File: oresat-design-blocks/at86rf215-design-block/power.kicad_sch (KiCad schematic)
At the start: 32 parts, among them J2 U.FL, J3 Conn_01x04, J4 Conn_01x04, J5 Conn_01x07, J6 Conn_01x10, U1 AT86RF215, Y1 TXETACSANF-26.000000

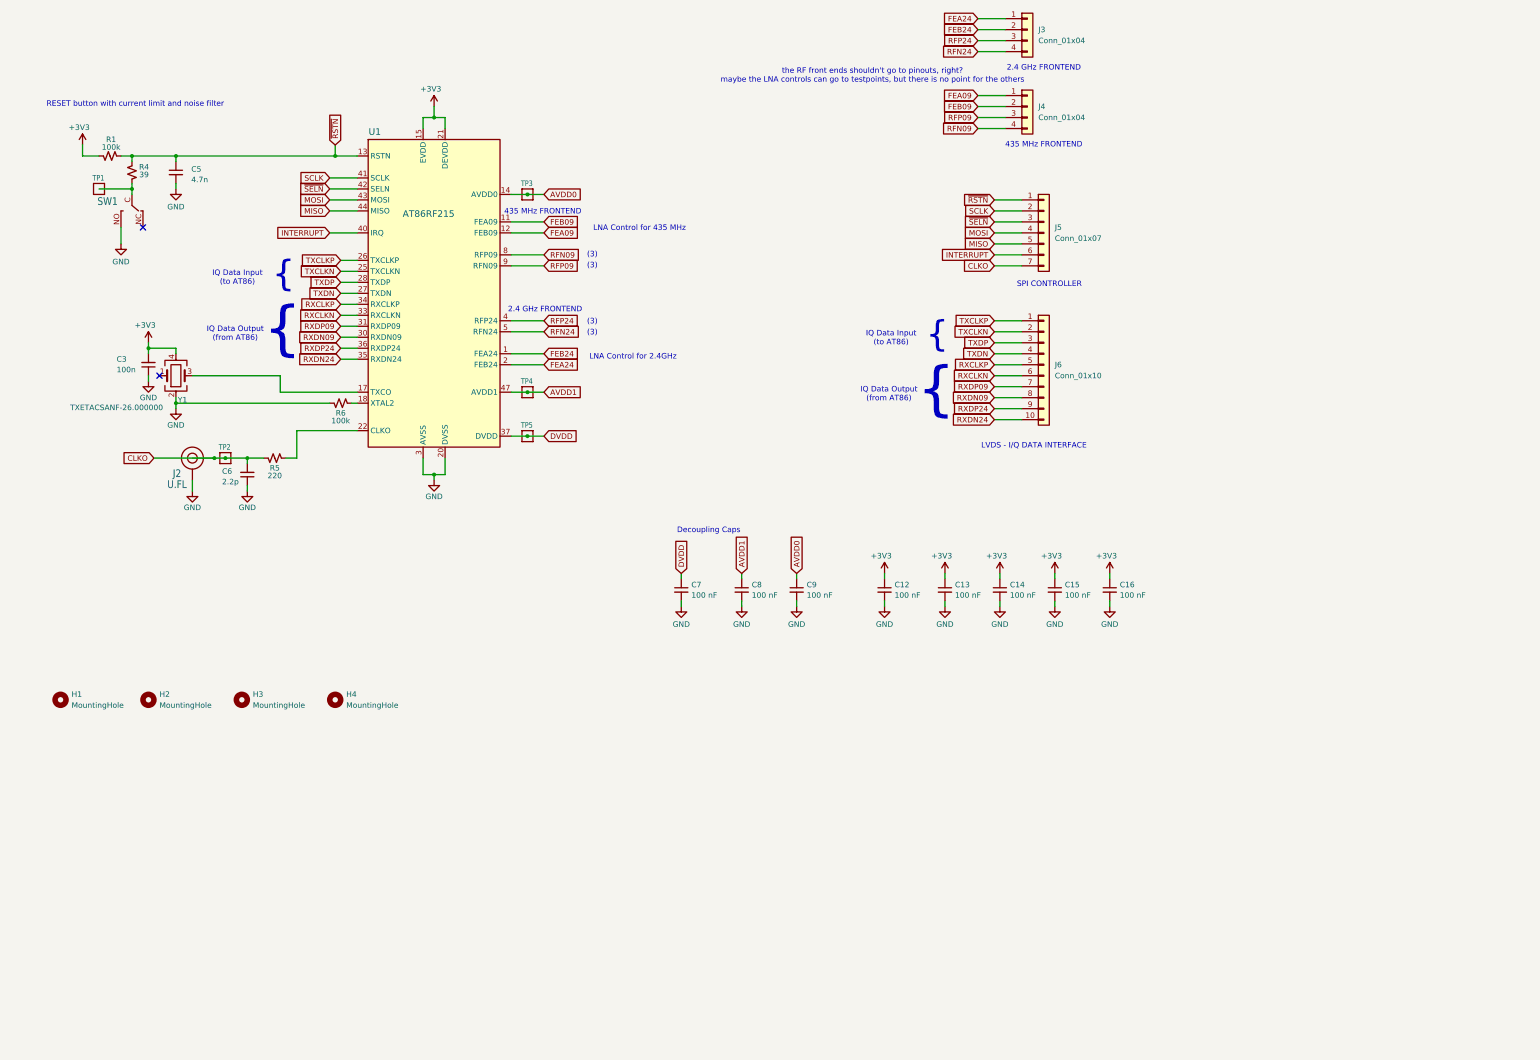
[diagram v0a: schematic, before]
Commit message: added initial footprints and oreganized schematic. Started PCB
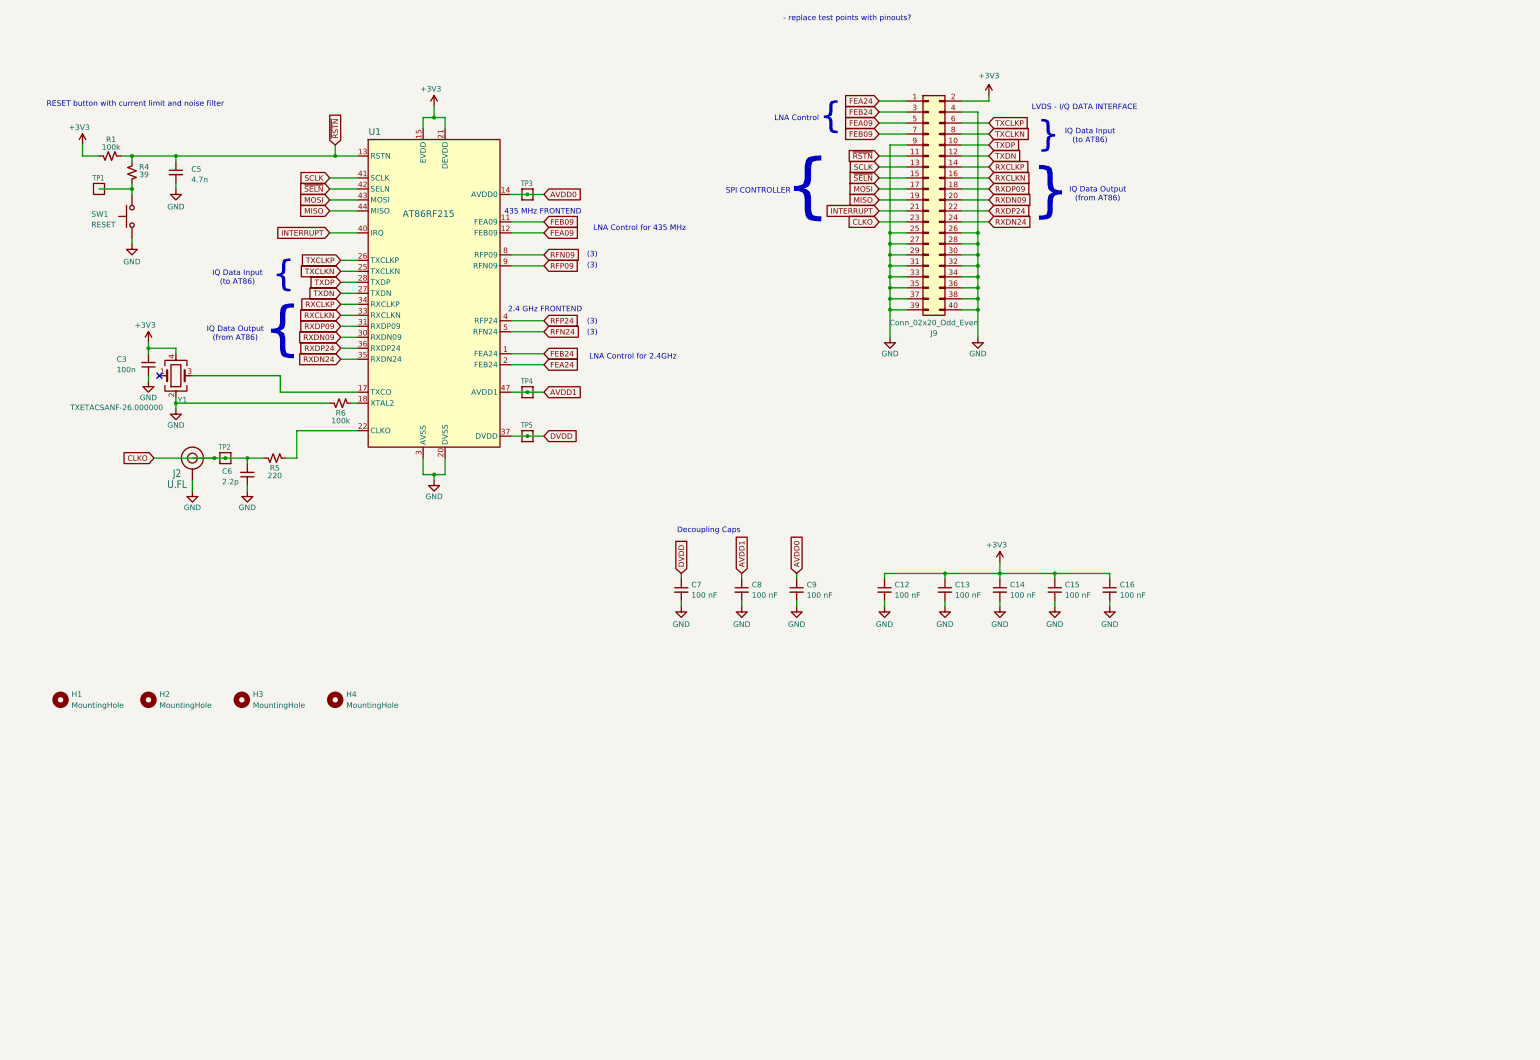
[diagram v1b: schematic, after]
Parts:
- removed J3, J4: Conn_01x04, symbol Connector_Generic:Conn_01x04
- removed J5: Conn_01x07, symbol Connector_Generic:Conn_01x07
- removed J6: Conn_01x10, symbol Connector_Generic:Conn_01x10
- removed SW1: ~, oresat-misc:D2F-L3-D-HORIZONTAL-R, symbol oresat-misc:OMRON-D2F-L3-D-RIGHT
- added J9: Conn_02x20_Odd_Even, Connector_PinHeader_2.54mm:PinHeader_2x20_P2.54mm_Vertical, symbol Connector_Generic:Conn_02x20_Odd_Even
- added SW1: RESET, Button_Switch_THT:SW_PUSH_6mm, symbol Switch:SW_Push
- C12, C13, C14, C15, C16, C3, C5, C6, C7, C8, C9: footprint (none) -> Capacitor_SMD:C_0603_1608Metric
- H1, H2, H3, H4: footprint (none) -> oresat-misc:M2-Press-Fit-Nut
- R1, R4, R5, R6: footprint (none) -> Resistor_SMD:R_0603_1608Metric
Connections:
- net +3V3: now also J9.2 (Pin_2)
- net AVSS: now also J9.25 (Pin_25), J9.26 (Pin_26), J9.27 (Pin_27), J9.28 (Pin_28), J9.29 (Pin_29), J9.30 (Pin_30), J9.31 (Pin_31), J9.32 (Pin_32), J9.33 (Pin_33), J9.34 (Pin_34), J9.35 (Pin_35), J9.36 (Pin_36), J9.37 (Pin_37), J9.38 (Pin_38), J9.39 (Pin_39), J9.4 (Pin_4), J9.40 (Pin_40), J9.9 (Pin_9), SW1.2
- net CLKO: now also J9.23 (Pin_23)
- net FEA09: now also J9.5 (Pin_5)
- net FEA24: now also J9.1 (Pin_1)
- net FEB09: now also J9.7 (Pin_7)
- net FEB24: now also J9.3 (Pin_3)
- net INTERRUPT: now also J9.21 (Pin_21)
- net MISO: now also J9.19 (Pin_19)
- net MOSI: now also J9.17 (Pin_17)
- net RXCLKN: now also J9.16 (Pin_16)
- net RXCLKP: now also J9.14 (Pin_14)
- net RXDN09: now also J9.20 (Pin_20)
- net RXDN24: now also J9.24 (Pin_24)
- net RXDP09: now also J9.18 (Pin_18)
- net RXDP24: now also J9.22 (Pin_22)
- net SCLK: now also J9.13 (Pin_13)
- net TXCLKN: now also J9.8 (Pin_8)
- net TXCLKP: now also J9.6 (Pin_6)
- net TXDN: now also J9.12 (Pin_12)
- net TXDP: now also J9.10 (Pin_10)
- net ~{RSTN}: now also J9.11 (Pin_11)
- net ~{SELN}: now also J9.15 (Pin_15)
- net at R4.2, TP1.1: now also SW1.1
- no-connect marks 2 -> 1
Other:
- note added: "- replace test points with pinouts?"
- note added: "LNA Control"
- note added: "}"
- note removed: "the RF front ends shouldn't go to pinouts, right? maybe the LNA controls can go to testpoints, but there is no point for the others"

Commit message: Pinout changes
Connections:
- net AVSS: now also J9.10 (Pin_10), J9.16 (Pin_16), J9.22 (Pin_22), J9.23 (Pin_23); no longer J9.25 (Pin_25), J9.26 (Pin_26), J9.30 (Pin_30), J9.32 (Pin_32)
- net CLKO: now also J9.25 (Pin_25); no longer J9.23 (Pin_23)
- net RXCLKN: now also J9.20 (Pin_20); no longer J9.16 (Pin_16)
- net RXCLKP: now also J9.18 (Pin_18); no longer J9.14 (Pin_14)
- net RXDN09: now also J9.26 (Pin_26); no longer J9.20 (Pin_20)
- net RXDN24: now also J9.32 (Pin_32); no longer J9.24 (Pin_24)
- net RXDP09: now also J9.24 (Pin_24); no longer J9.18 (Pin_18)
- net RXDP24: now also J9.30 (Pin_30); no longer J9.22 (Pin_22)
- net TXDN: now also J9.14 (Pin_14); no longer J9.12 (Pin_12)
- net TXDP: now also J9.12 (Pin_12); no longer J9.10 (Pin_10)

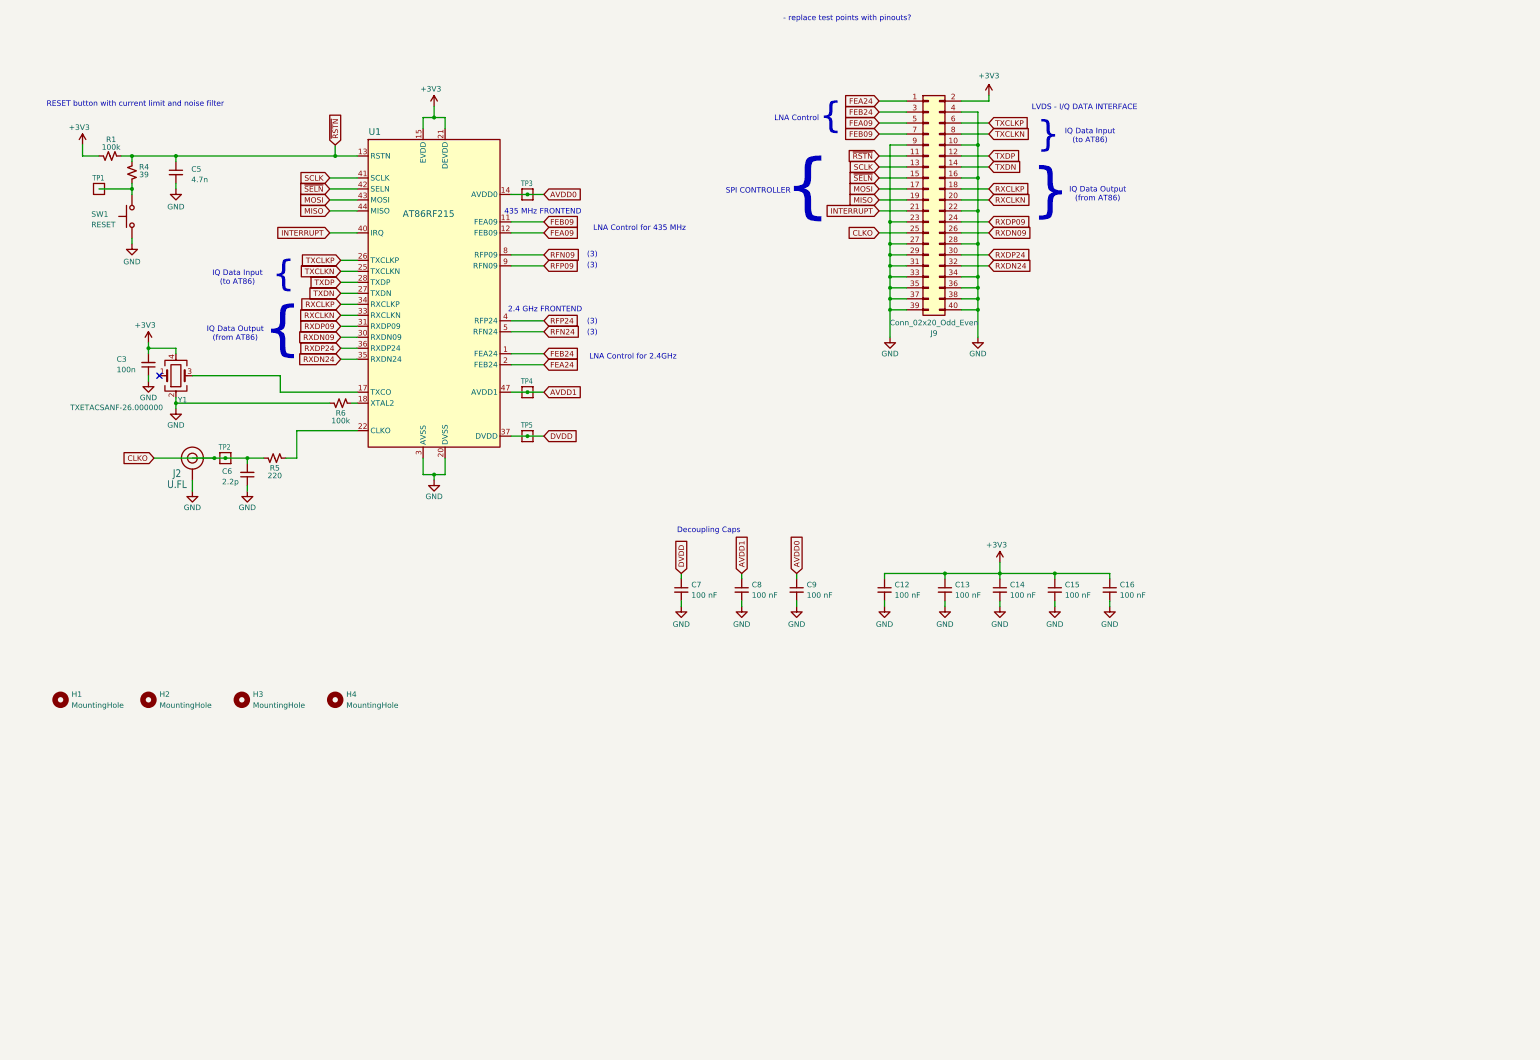
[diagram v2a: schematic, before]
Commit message: First design review of AT86 eval board. Added 5V to 3.3V LDO with low noise, added USB C port, and found a Balun for UHF and L band.
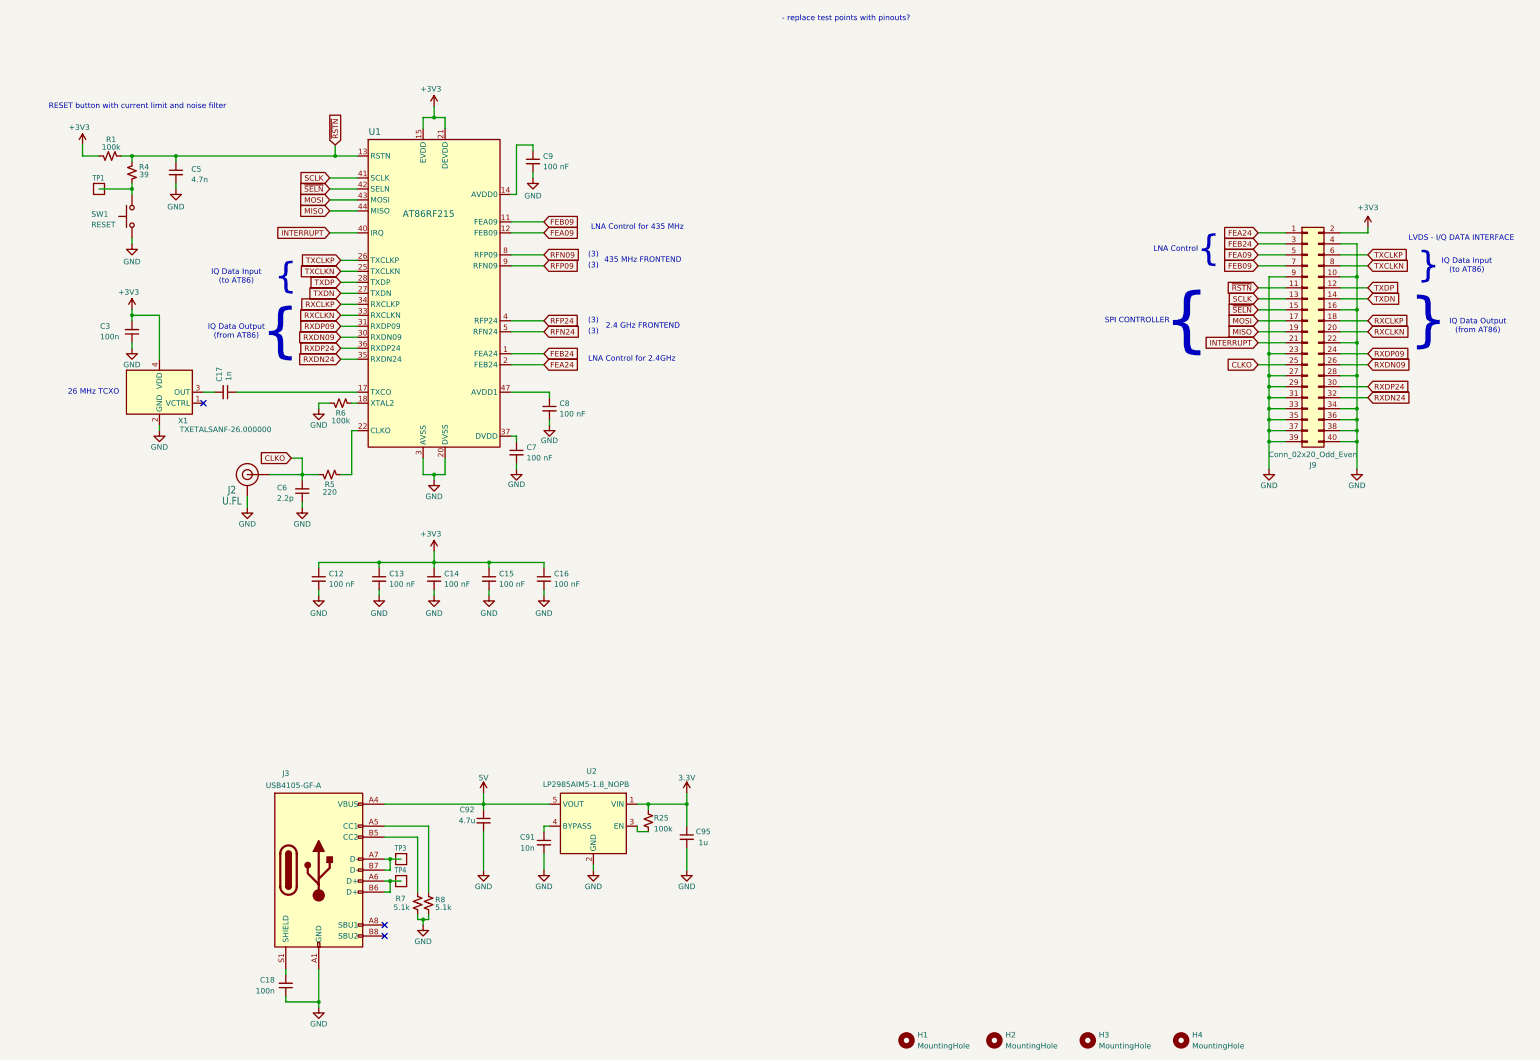
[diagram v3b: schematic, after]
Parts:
- removed TP2, TP5: ~, oresat-misc:TestPoint_Pad_D1.0mm, symbol oresat-misc:Test-Point-1mm-round
- removed Y1: TXETACSANF-26.000000, Crystal:Crystal_SMD_Abracon_ABM8AIG-4Pin_3.2x2.5mm, symbol Device:Crystal_GND24
- added C17: 1n, Capacitor_SMD:C_0603_1608Metric, symbol Device:C_Small
- added C18: 100n, oresat-passives:0603-C-NOSILK, symbol Device:C_Small
- added C91: 10n, Capacitor_SMD:C_0603_1608Metric, symbol Device:C_Small
- added C92: 4.7u, Capacitor_SMD:C_0603_1608Metric, symbol Device:C_Small
- added C95: 1u, Capacitor_SMD:C_0603_1608Metric, symbol Device:C_Small
- added J3: USB4105-GF-A, Connector_USB:USB_C_Receptacle_Palconn_UTC16-G, symbol Connector:USB_C_Receptacle_USB2.0_16P
- added R25: 100k, Resistor_SMD:R_0603_1608Metric, symbol Device:R_Small_US
- added R7, R8: 5.1k, oresat-passives:0603-C-NOSILK, symbol Device:R_Small_US
- added U2: LP2985AIM5-1.8_NOPB, Package_TO_SOT_SMD:SOT-23-5, symbol oresat-ics:LP2985-N
- added X1: TXETALSANF-26.000000, oresat-ics:X_TCXO_SMD_Taitien_2.5x2.0mm, symbol oresat-ics:Taiten-TY-Series-TXCO
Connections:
- net +3V3: now also X1.4 (VDD)
- net AVSS: now also C18.1, C91.2, C92.2, C95.2, J3.A1 (GND), J3.A12 (GND), J3.B1 (GND), J3.B12 (GND), R7.2, R8.2, U2.2 (GND), X1.2 (GND)
- net at U1.17 (TXCO): now also C17.1
- net AVDD0: no longer names the net of C9.1, U1.14 (AVDD0)
- net AVDD0: no longer TP3.1
- net AVDD1: no longer names the net of C8.1, U1.47 (AVDD1)
- net AVDD1: no longer TP4.1
- net DVDD: no longer names the net of C7.1, U1.37 (DVDD)
- new net: C18.2, J3.S1 (SHIELD)
- new net: R25.2, U2.3 (EN)
- new net: J3.A5 (CC1), R8.1
- new net: J3.A6 (D+), J3.B6 (D+), TP4.1
- new net: J3.A7 (D-), J3.B7 (D-), TP3.1
- new net: J3.B5 (CC2), R7.1
- new net: C91.1, U2.4 (BYPASS)
- new net: C17.2, X1.3 (OUT)
- new net 3.3V: C95.1, R25.1, U2.1 (VIN)
- new net 5V: C92.1, J3.A4 (VBUS), J3.A9 (VBUS), J3.B4 (VBUS), J3.B9 (VBUS), U2.5 (VOUT)
- no-connect marks 1 -> 3
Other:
- note added: "26 MHz TCXO"
- note removed: "Decoupling Caps"
- company: (none) -> Portland State Aerospace Society
- title: (none) -> OreSat AT86RF215 Evaluation Board
- moved on the sheet: C12, C13, C14, C15, C16, C3, C6, C7, C8, C9, H1, H2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

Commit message: added initial 436.5mhz circuit
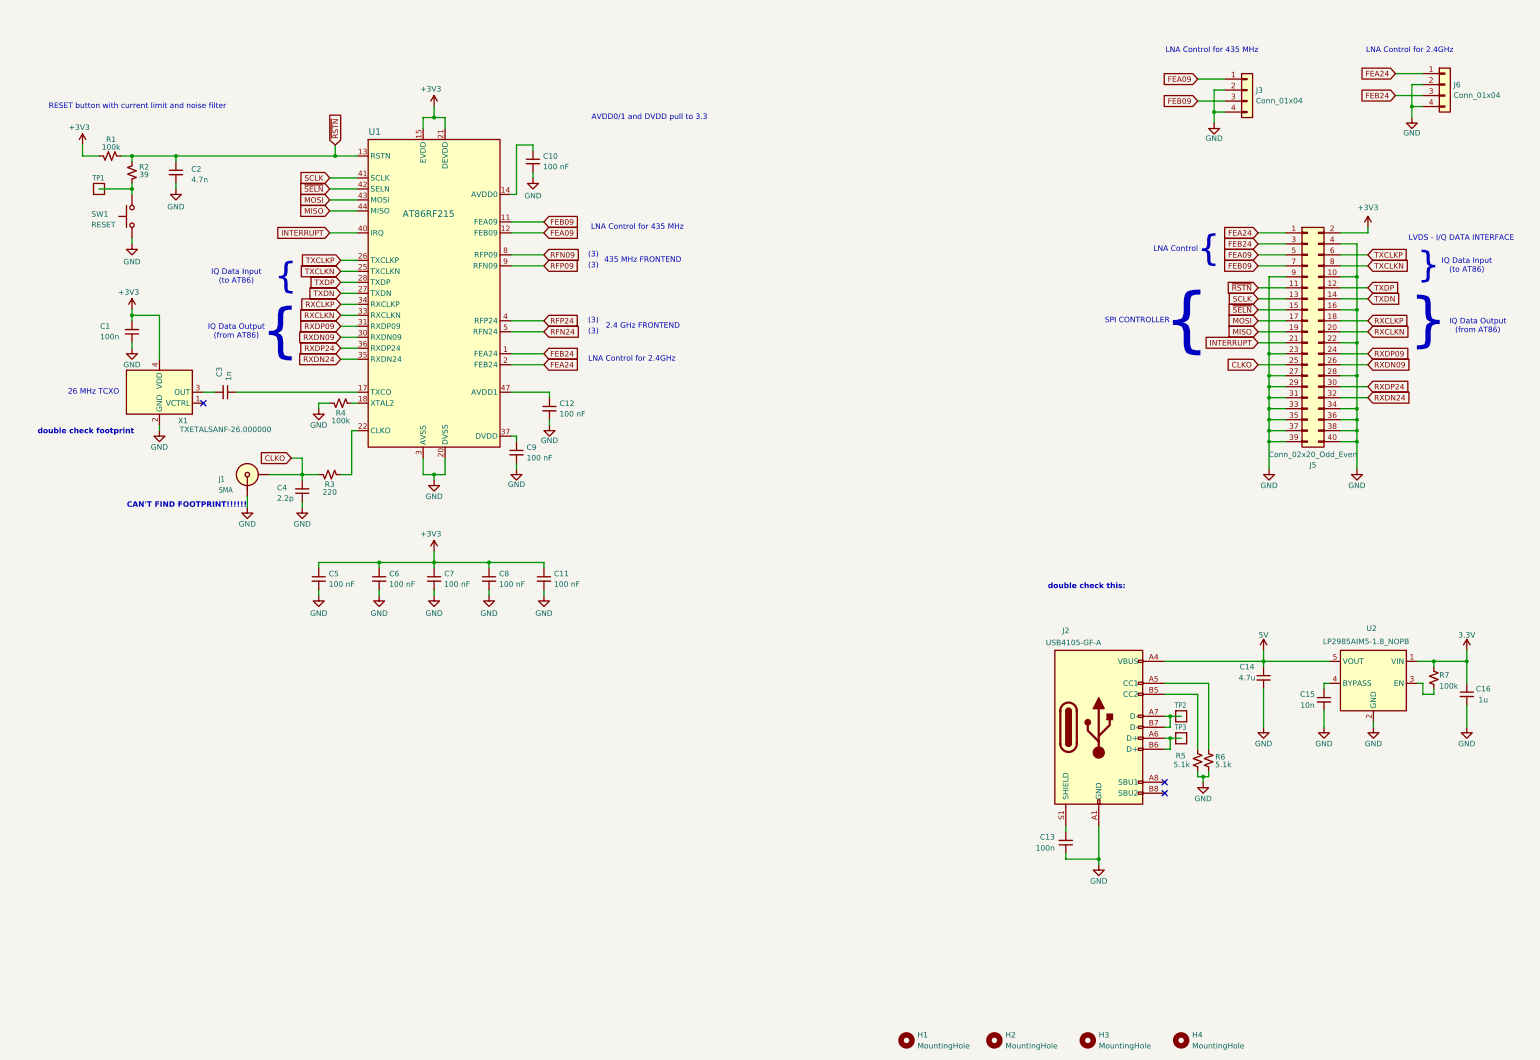
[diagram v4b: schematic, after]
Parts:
- removed J2: U.FL, oresat-minusz-end-card:U.FL, symbol oresat-connectors:U.FL2PIN
- added J1: SMA, Connector_Coaxial:SMA_Samtec_SMA-J-P-H-ST-EM1_EdgeMount, symbol oresat-connectors:J-MOLEX-SMPM-73300-002X
- added J3, J6: Conn_01x04, symbol Connector_Generic:Conn_01x04
- renumbered C3 to C1, C9 to C10, C16 to C11, C8 to C12, C18 to C13, C92 to C14, C91 to C15, C95 to C16, C5 to C2, C17 to C3, C6 to C4, C12 to C5, C13 to C6, C14 to C7, C15 to C8, C7 to C9, J3 to J2, J9 to J5, R4 to R2, R5 to R3, R6 to R4, R7 to R5, R8 to R6, R25 to R7, TP3 to TP2, TP4 to TP3
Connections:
- net AVSS: now also J1.SIG, J3.2 (Pin_2), J3.4 (Pin_4), J6.2 (Pin_2), J6.4 (Pin_4)
- net CLKO: now also J1.SHLD
- net FEA09: now also J3.1 (Pin_1)
- net FEA24: now also J6.1 (Pin_1)
- net FEB09: now also J3.3 (Pin_3)
- net FEB24: now also J6.3 (Pin_3)
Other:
- note added: "AVDD0/1 and DVDD pull to 3.3"
- note added: "CAN'T FIND FOOTPRINT!!!!!!"
- note added: "double check footprint"
- note added: "double check this:"
- note removed: "- replace test points with pinouts?"
- moved on the sheet: C13, C14, C15, C16, J2, R5, R6, R7, TP2, TP3, U2
